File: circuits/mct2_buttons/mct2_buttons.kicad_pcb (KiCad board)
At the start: 2 copper layers, 62.5 x 28 mm, 35 parts, among them J1 Conn_01x08, SW1 B3F-1052, SW10 B3F-1052, SW11 B3F-1052, SW12 B3F-1052, SW13 OS102011MS2QN1C, SW14 OS102011MS2QN1C, SW2 B3F-1052, SW3 B3F-1052, SW4 B3F-1052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

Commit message: Aug 3, 2024
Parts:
- removed H4: MountingHole, MountingHole:MountingHole_2.2mm_M2_Pad
- added H3: MountingHole, MountingHole:MountingHole_2.2mm_M2_Pad, F.Cu at (98.0, 65.0)
- moved H2 63.9 mm to (98.0, 43.0)
- moved J1 47.7 mm to (44.9, 54.0), turned to -90 degrees
- moved C1 37.6 mm to (51.9, 53.1)
- moved R2 37.0 mm to (49.1, 53.0)
- moved SW13 36.5 mm to (52.5, 63.0)
- moved SW14 36.5 mm to (52.5, 43.0)
- moved C2 36.0 mm to (48.0, 58.3)
- moved R1 35.0 mm to (51.9, 56.7), turned to 90 degrees
- moved U1 23.5 mm to (56.2, 54.1), turned to 90 degrees
- moved D1 23.2 mm to (66.2, 48.5), turned to 0 degrees
- moved D2 23.2 mm to (66.2, 57.5), turned to 0 degrees
- moved D3 23.2 mm to (66.2, 66.5), turned to 0 degrees
- moved D4 23.2 mm to (75.2, 48.5), turned to 0 degrees
- moved D5 23.2 mm to (75.2, 57.5), turned to 0 degrees
- moved D6 23.2 mm to (75.2, 66.5), turned to 0 degrees
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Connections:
- net Net-(D11-K) renamed COL1
- D1 pad 1: Net-(D1-K) -> COL2
- D10 pad 1: Net-(D1-K) -> COL2
- D12 pad 1: Net-(D12-K) -> COL0
- D3 pad 1: Net-(D12-K) -> COL0
- D4 pad 1: Net-(D1-K) -> COL2
- D6 pad 1: Net-(D12-K) -> COL0
- D7 pad 1: Net-(D1-K) -> COL2
- D9 pad 1: Net-(D12-K) -> COL0
- U1 pad 11: Net-(D12-K) -> COL2
- U1 pad 9: Net-(D1-K) -> COL0
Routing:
- net Net-(D12-K): track 47.7 -> 0.00 mm
- net COL0: track 0.00 -> 46.3 mm
- net COL2: track 0.00 -> 40.6 mm
- net Net-(D1-K): track 38.7 -> 0.00 mm
- net Net-(U1-ROW4): track 64.2 -> 35.9 mm, vias 0 -> 1
- net Net-(U1-ROW7): track 38.8 -> 65.9 mm, vias 0 -> 1
- net VCC: track 46.8 -> 32.7 mm, vias 3 -> 2
- net Net-(U1-ROW5): track 55.7 -> 45.6 mm, vias 0 -> 1
- net Net-(U1-ROW6): track 47.4 -> 55.5 mm, vias 0 -> 1
- net Net-(J1-Pin_2): track 23.3 -> 20.7 mm
- net Net-(J1-Pin_5): track 10.5 -> 8.67 mm
- net Net-(J1-Pin_6): track 10.3 -> 8.72 mm
- net Net-(J1-Pin_7): track 10.1 -> 8.92 mm
- net Net-(J1-Pin_4): track 10.6 -> 9.45 mm
- net GND: track 7.21 -> 6.33 mm, vias 71 -> 78
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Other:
- board size 62.5 x 28 mm -> 61 x 28 mm
- board text added: "MediaCow Touch 2 Button Board Rev.B 20240803 CTCL 2021-2024"
- board text removed: "MediaCow Touch 2 Button Board Rev.A 20240801 CTCL 2021-2024"

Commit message: Aug 7, 2024 stuff in case I don't work on this before going to FMB
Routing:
- net GND: vias 78 -> 80
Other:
- board text added: "MediaCow Touch 2 Button Board Rev.B 20240805 CTCL 2021-2024"
- board text removed: "MediaCow Touch 2 Button Board Rev.B 20240803 CTCL 2021-2024"

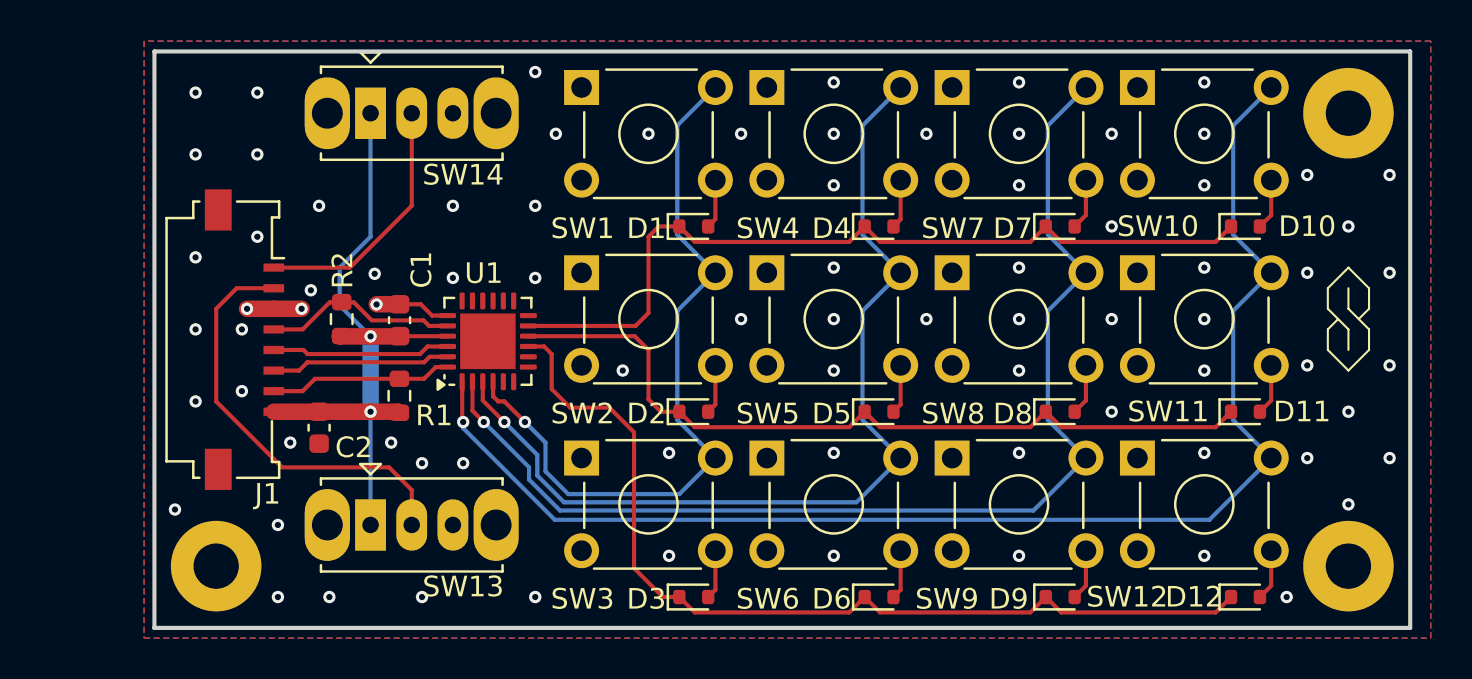
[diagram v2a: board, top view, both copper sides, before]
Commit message: 20250220-1 Add GOWIN FPGA symbol
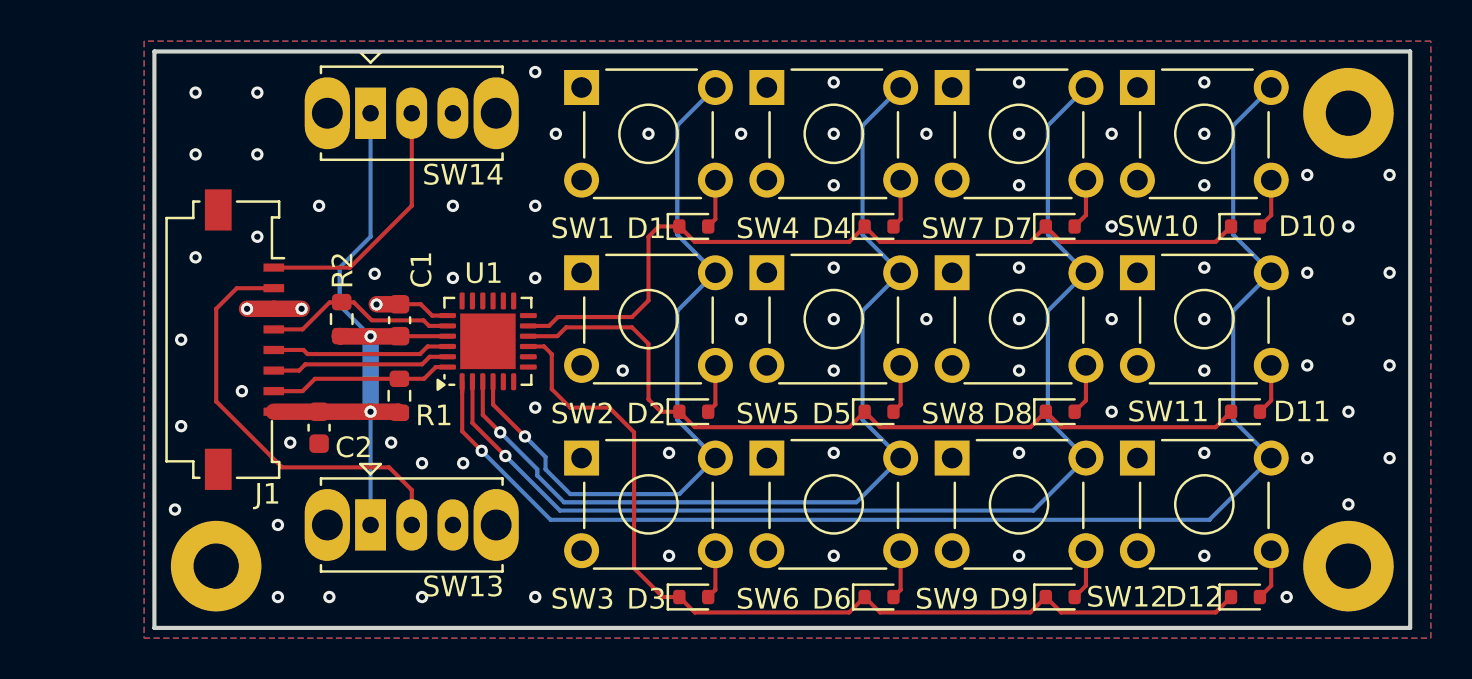
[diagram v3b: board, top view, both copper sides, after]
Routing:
- net COL1: track 38.9 -> 39.5 mm
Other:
- board text added: "MediaCow Touch 2 Button Board 20250216 CTCL 2021-2025"
- board text removed: "MediaCow Touch 2 Button Board Rev.B 20240805 CTCL 2021-2024"
